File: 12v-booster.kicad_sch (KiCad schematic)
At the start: 20 parts, among them J201 12V_OUT, U201 TPS61089RNRR, U202 MPM3810GQB-33

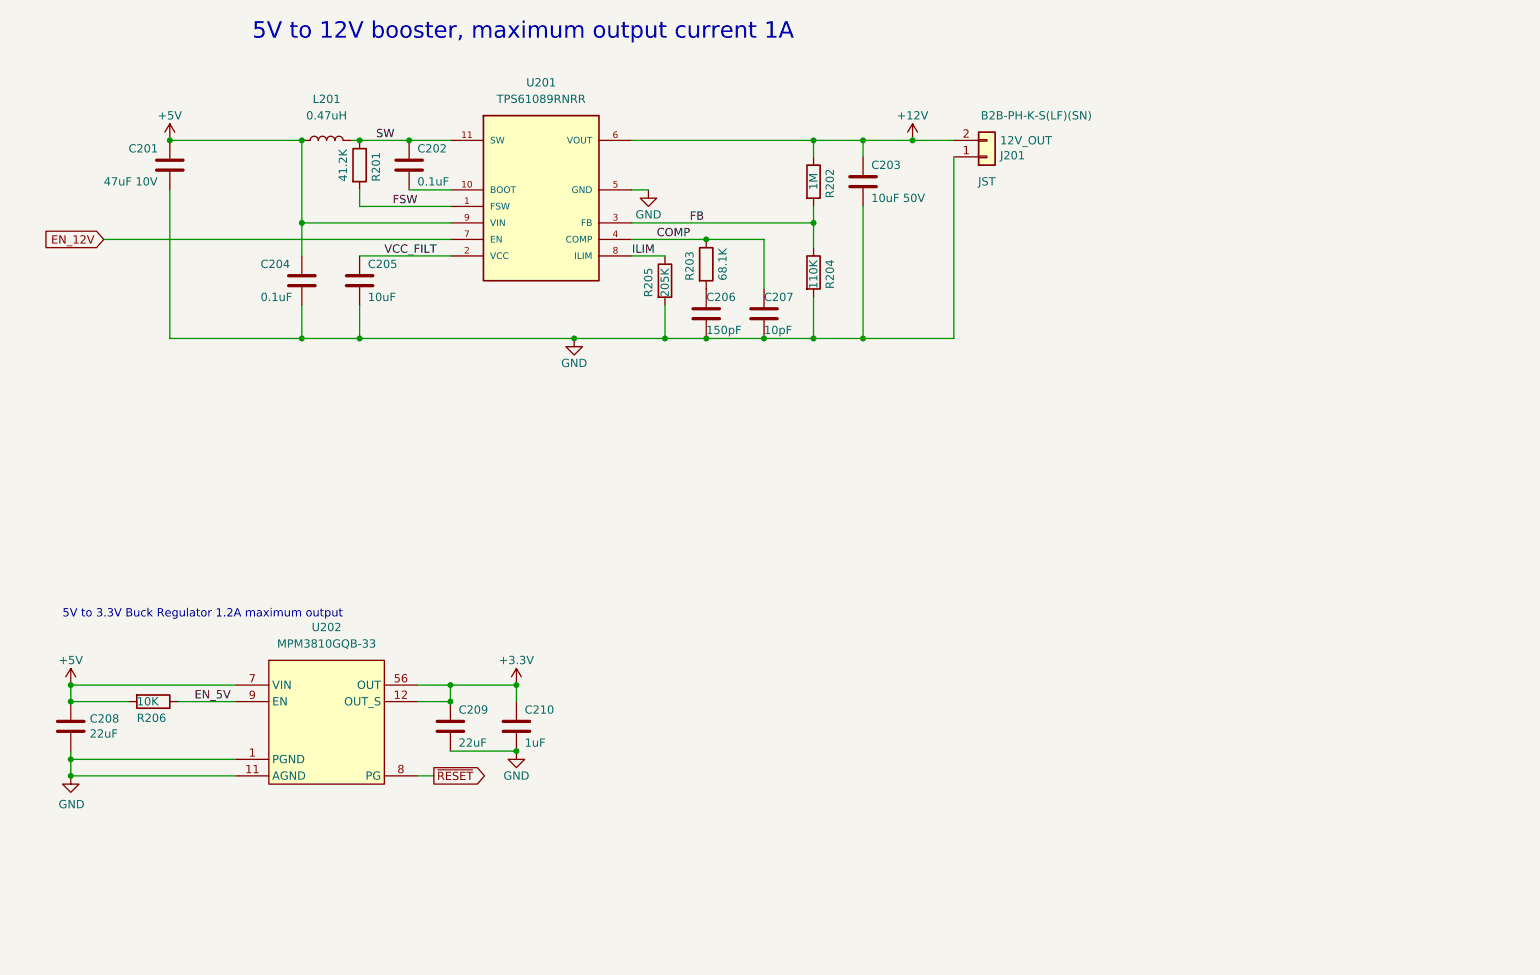
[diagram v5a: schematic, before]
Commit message: Moved to ESP32 S3 Wroom 1
The Wroom 2 requires 1.8V on a couple of GPIOs.  Since I don't need 32MB of
flash the Wroom 1 is used instead.  The footprint is slightly different,
however.

Signed-off-by: Aaron Williams <aaron.w2@gmail.com>
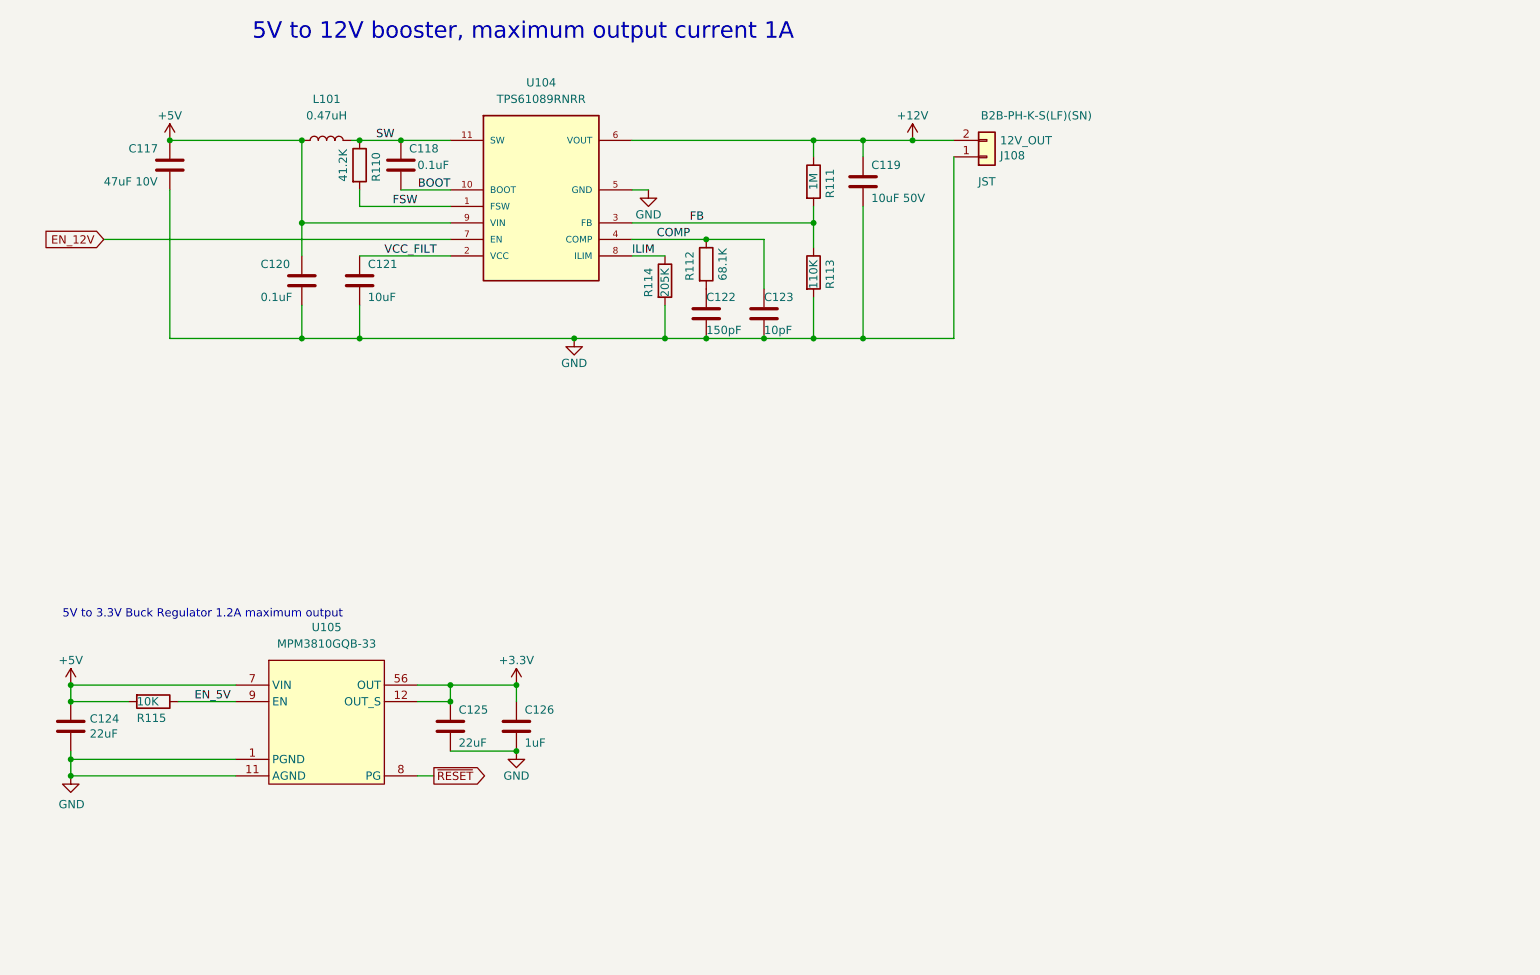
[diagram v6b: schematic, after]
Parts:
- C122: renamed from C206; MFR (none) -> Samsung Electro-Mechanics; MPN (none) -> CL05C151JB5NNNC; Manufacturer Part Number (none) -> CL05C151JB5NNNC; SPN (none) -> 1276-1046-1-ND; SPURL (none) -> https://www.digikey.com/en/products/detail/samsung-electro-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
- C123: renamed from C207; MFR (none) -> TDK Corporation; MPN (none) -> CGA2B2NP01H100D050BA; Manufacturer Part Number (none) -> CGA2B2NP01H100D050BA; SPN (none) -> 445-12120-1-ND; SPURL (none) -> https://www.digikey.com/en/products/detail/tdk-corporation/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
- renumbered C201 to C117, C202 to C118, C203 to C119, C204 to C120, C205 to C121, C208 to C124, C209 to C125, C210 to C126, J201 to J108, L201 to L101, R201 to R110, R202 to R111, R203 to R112, R204 to R113, R205 to R114, R206 to R115, U201 to U104, U202 to U105
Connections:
- net BOOT: now reaches C118.2, U104.10 (BOOT)
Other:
- moved on the sheet: C118
